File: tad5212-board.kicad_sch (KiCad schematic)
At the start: 11 parts, among them J1 Conn_01x10, J2 Conn_01x10, U1 XTAD5212IRGER

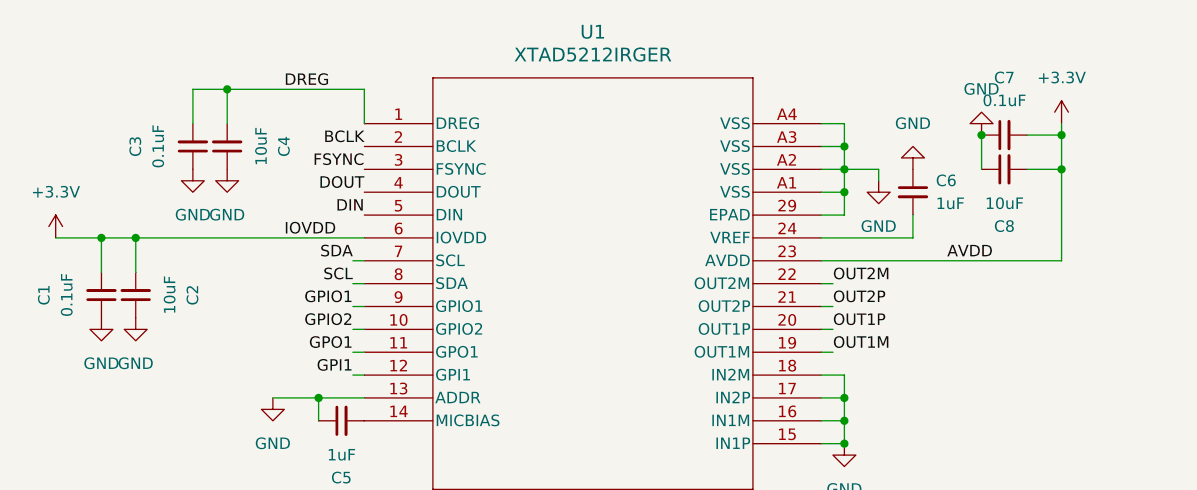
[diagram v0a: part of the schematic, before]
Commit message: v2 with hive compat footprints and fix i2c
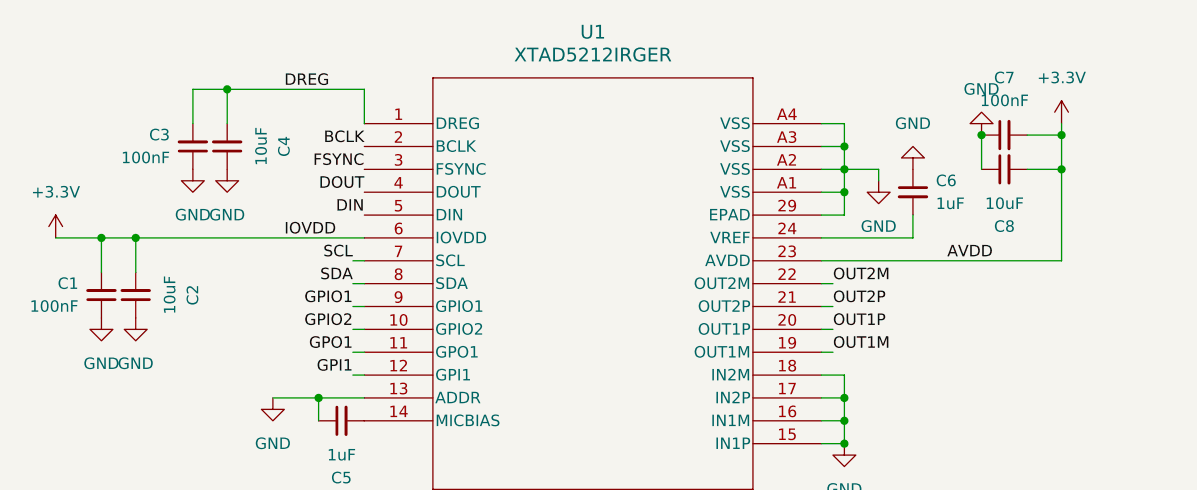
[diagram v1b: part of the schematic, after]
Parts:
- C1, C3, C7: value 0.1uF -> 100nF
- C2, C4, C8: footprint Capacitor_SMD:C_0603_1608Metric -> Capacitor_SMD:C_0805_2012Metric
- J1, J2: LCSC PN (none) -> C5383117
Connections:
- net SCL: now also U1.7 (SCL); no longer U1.8 (SDA)
- net SDA: now also U1.8 (SDA); no longer U1.7 (SCL)
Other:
- moved on the sheet: C1, C3

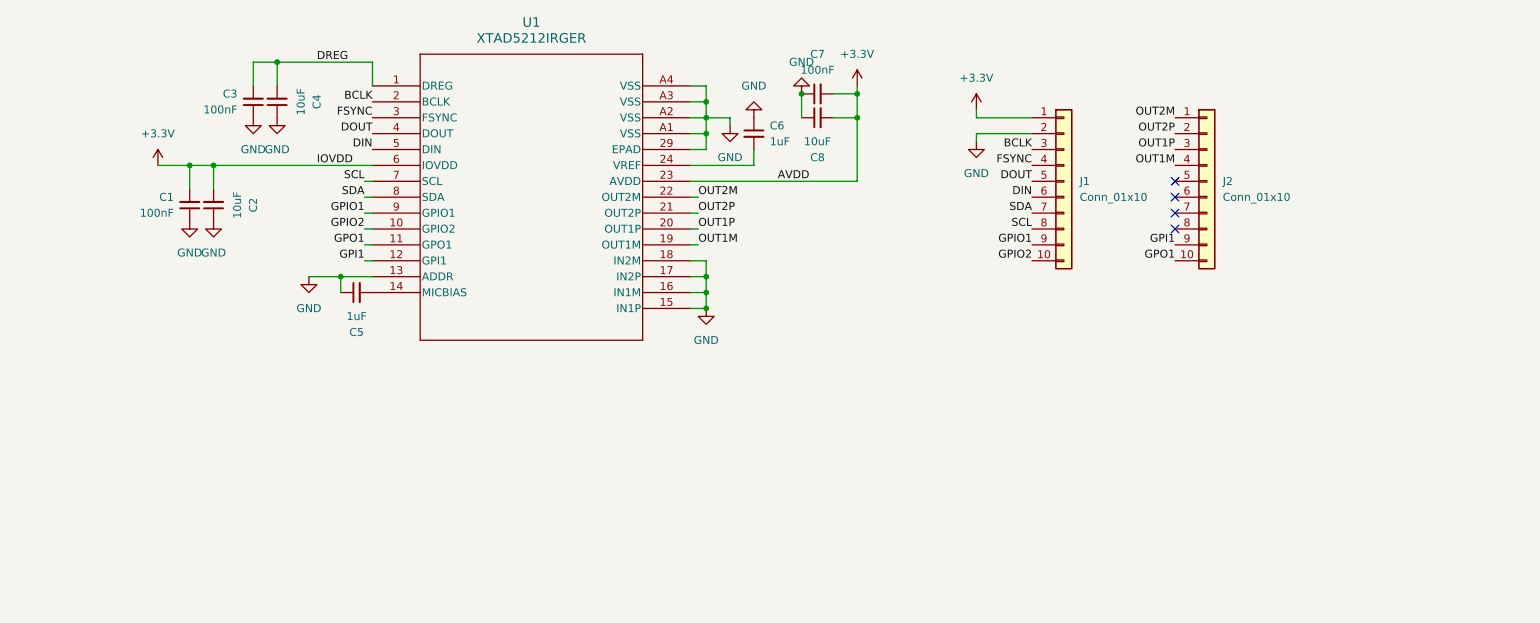
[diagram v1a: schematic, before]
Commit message: make 4-layer; add ldo
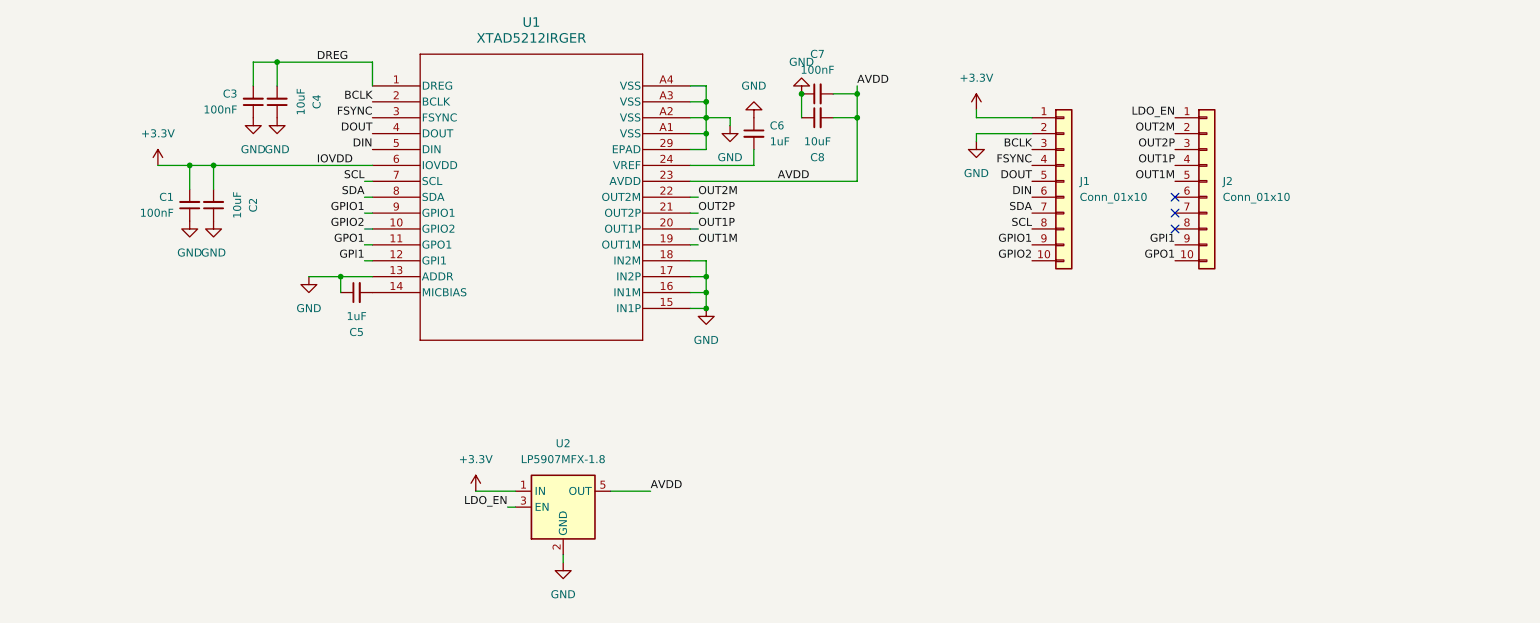
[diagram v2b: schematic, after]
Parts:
- added U2: LP5907MFX-1.8, Package_TO_SOT_SMD:SOT-23-5, symbol Regulator_Linear:LP5907MFX-1.8
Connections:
- net +3.3V: now also U2.1 (IN); no longer C7.2, C8.2, U1.23 (AVDD)
- net GND: now also U2.2 (GND)
- net OUT1M: now also J2.5 (Pin_5); no longer J2.4 (Pin_4)
- net OUT1P: now also J2.4 (Pin_4); no longer J2.3 (Pin_3)
- net OUT2M: now also J2.2 (Pin_2); no longer J2.1 (Pin_1)
- net OUT2P: now also J2.3 (Pin_3); no longer J2.2 (Pin_2)
- new net AVDD: C7.2, C8.2, U1.23 (AVDD), U2.5 (OUT)
- new net LDO_EN: J2.1 (Pin_1), U2.3 (EN)
- no-connect marks 4 -> 3

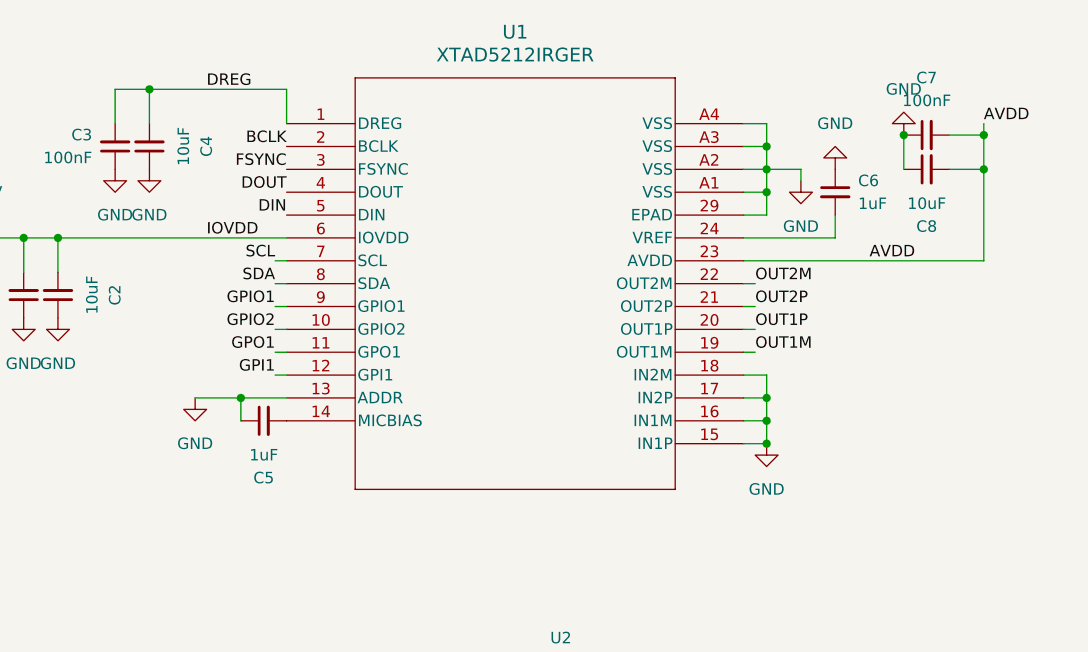
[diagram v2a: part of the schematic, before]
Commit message: add via stitching
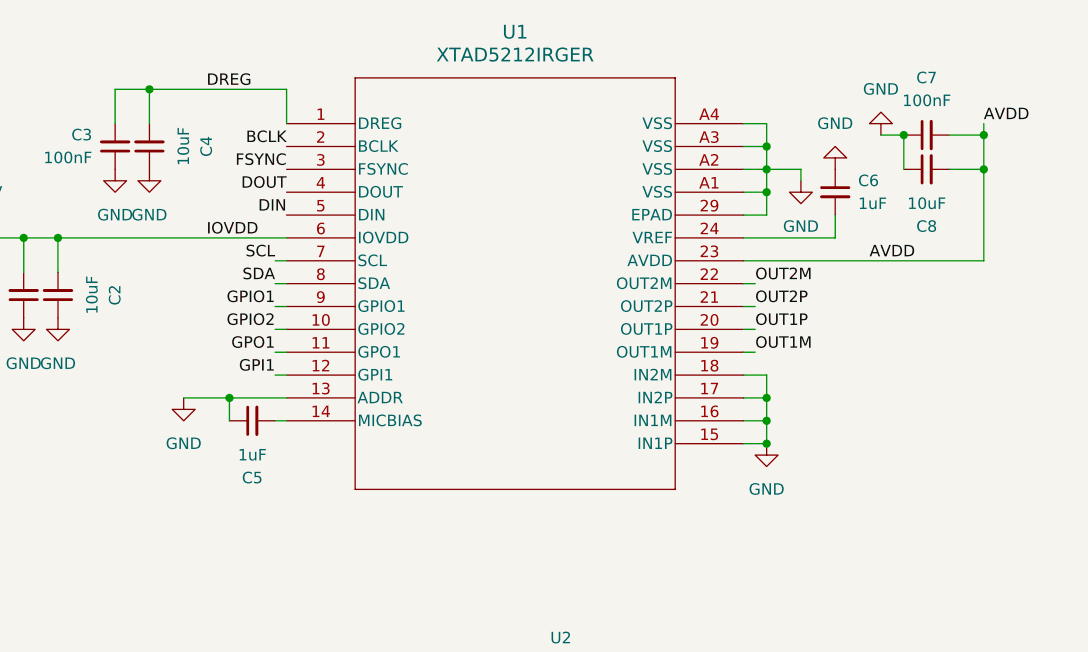
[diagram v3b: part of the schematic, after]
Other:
- moved on the sheet: C5
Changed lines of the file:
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@@
 	(paper "A4")
+	(junction
+		(at 57.15 64.77)
+		(diameter 0)
+		(color 0 0 0 0)
+	)
+	(junction
+		(at 60.96 64.77)
+		(diameter 0)
+		(color 0 0 0 0)
+	)
+	(junction
+		(at 163.83 57.15)
+		(diameter 0)
+		(color 0 0 0 0)
+	)
+	(junction
+		(at 139.7 57.15)
+		(diameter 0)
+		(color 0 0 0 0)
+	)
+	(junction
+		(at 139.7 85.09)
+		(diameter 0)
+		(color 0 0 0 0)
+	)
+	(junction
+		(at 139.7 59.69)
+		(diameter 0)
+		(color 0 0 0 0)
+	)
+	(junction
+		(at 139.7 82.55)
+		(diameter 0)
+		(color 0 0 0 0)
+	)
+	(junction
+		(at 80.01 82.55)
+		(diameter 0)
+		(color 0 0 0 0)
+	)
+	(junction
+		(at 139.7 87.63)
+		(diameter 0)
+		(color 0 0 0 0)
+	)
+	(junction
+		(at 163.83 53.34)
+		(diameter 0)
+		(color 0 0 0 0)
+	)
+	(junction
+		(at 71.12 48.26)
+		(diameter 0)
+		(color 0 0 0 0)
+	)
 	(junction
 		(at 154.94 53.34)
@@
 	)
 	(junction
-		(at 57.15 64.77)
-		(diameter 0)
-		(color 0 0 0 0)
-	)
-	(junction
-		(at 60.96 64.77)
-		(diameter 0)
-		(color 0 0 0 0)
-	)
-	(junction
-		(at 163.83 57.15)
-		(diameter 0)
-		(color 0 0 0 0)
-	)
-	(junction
-		(at 139.7 57.15)
-		(diameter 0)
-		(color 0 0 0 0)
-	)
-	(junction
-		(at 139.7 85.09)
-		(diameter 0)
-		(color 0 0 0 0)
-	)
-	(junction
-		(at 139.7 59.69)
-		(diameter 0)
-		(color 0 0 0 0)
-	)
-	(junction
-		(at 139.7 82.55)
-		(diameter 0)
-		(color 0 0 0 0)
-	)
-	(junction
-		(at 81.28 82.55)
-		(diameter 0)
-		(color 0 0 0 0)
-	)
-	(junction
-		(at 139.7 87.63)
-		(diameter 0)
-		(color 0 0 0 0)
-	)
-	(junction
-		(at 163.83 53.34)
-		(diameter 0)
-		(color 0 0 0 0)
-	)
-	(junction
-		(at 71.12 48.26)
-		(diameter 0)
-		(color 0 0 0 0)
-	)
-	(junction
 		(at 139.7 54.61)
 		(diameter 0)
@@
 	(wire
 		(pts
-			(xy 81.28 82.55) (xy 81.28 85.09)
+			(xy 80.01 82.55) (xy 80.01 85.09)
 		)
 		(stroke
@@
 	(wire
 		(pts
-			(xy 81.28 82.55) (xy 86.36 82.55)
+			(xy 80.01 82.55) (xy 86.36 82.55)
 		)
 		(stroke
@@
 	(wire
 		(pts
-			(xy 76.2 82.55) (xy 81.28 82.55)
+			(xy 74.93 82.55) (xy 80.01 82.55)
 		)
 		(stroke
@@
 	(wire
 		(pts
+			(xy 85.09 85.09) (xy 86.36 85.09)
+		)
+		(stroke
+			(width 0)
+			(type default)
+		)
+	)
+	(wire
+		(pts
 			(xy 60.96 64.77) (xy 86.36 64.77)
 		)
@@
 		(pts
 			(xy 60.96 64.77) (xy 60.96 68.58)
+		)
+		(stroke
+			(width 0)
+			(type default)
+		)
+	)
+	(wire
+		(pts
+			(xy 152.4 53.34) (xy 154.94 53.34)
 		)
 		(stroke
@@
 	(symbol
 		(lib_id "power:GND")
-		(at 154.94 53.34 180)
+		(at 152.4 53.34 180)
 		(unit 1)
 		(body_style 1)
@@
 		(fields_autoplaced yes)
 		(property "Reference" "#PWR013"
-			(at 154.94 46.99 0)
+			(at 152.4 46.99 0)
 			(hide yes)
 			(show_name no)
@@
 		)
 		(property "Value" "GND"
-			(at 154.94 48.26 0)
+			(at 152.4 48.26 0)
 			(show_name no)
 			(do_not_autoplace no)
@@
 		)
 		(property "Footprint" ""
-			(at 154.94 53.34 0)
+			(at 152.4 53.34 0)
 			(hide yes)
 			(show_name no)
@@
 		)
 		(property "Datasheet" ""
-			(at 154.94 53.34 0)
+			(at 152.4 53.34 0)
 			(hide yes)
 			(show_name no)
@@
 		)
 		(property "Description" "Power symbol creates a global label with name \"GND\" , ground"
-			(at 154.94 53.34 0)
+			(at 152.4 53.34 0)
 			(hide yes)
 			(show_name no)
@@
 	(symbol
 		(lib_id "Device:C_Small")
-		(at 83.82 85.09 90)
+		(at 82.55 85.09 90)
 		(mirror x)
 		(unit 1)
@@
 		(fields_autoplaced yes)
 		(property "Reference" "C5"
-			(at 83.8263 91.44 90)
+			(at 82.5563 91.44 90)
 			(show_name no)
 			(do_not_autoplace no)
@@
 		)
 		(property "Value" "1uF"
-			(at 83.8263 88.9 90)
+			(at 82.5563 88.9 90)
 			(show_name no)
 			(do_not_autoplace no)
@@
 		)
 		(property "Footprint" "Capacitor_SMD:C_0603_1608Metric"
-			(at 83.82 85.09 0)
+			(at 82.55 85.09 0)
 			(hide yes)
 			(show_name no)
@@
 		)
 		(property "Datasheet" ""
-			(at 83.82 85.09 0)
+			(at 82.55 85.09 0)
 			(hide yes)
 			(show_name no)
@@
 		)
 		(property "Description" "Unpolarized capacitor, small symbol"
-			(at 83.82 85.09 0)
+			(at 82.55 85.09 0)
 			(hide yes)
 			(show_name no)
@@
 	(symbol
 		(lib_id "power:GND")
-		(at 76.2 82.55 0)
+		(at 74.93 82.55 0)
 		(unit 1)
 		(body_style 1)
@@
 		(fields_autoplaced yes)
 		(property "Reference" "#PWR06"
-			(at 76.2 88.9 0)
+			(at 74.93 88.9 0)
 			(hide yes)
 			(show_name no)
@@
 		)
 		(property "Value" "GND"
-			(at 76.2 87.63 0)
+			(at 74.93 87.63 0)
 			(show_name no)
 			(do_not_autoplace no)
@@
 		)
 		(property "Footprint" ""
-			(at 76.2 82.55 0)
+			(at 74.93 82.55 0)
 			(hide yes)
 			(show_name no)
@@
 		)
 		(property "Datasheet" ""
-			(at 76.2 82.55 0)
+			(at 74.93 82.55 0)
 			(hide yes)
 			(show_name no)
@@
 		)
 		(property "Description" "Power symbol creates a global label with name \"GND\" , ground"
-			(at 76.2 82.55 0)
-			(hide yes)
-			(show_name no)
+			(at 74.93 82.55 0)
+			(hide yes)
+			(show_name no)

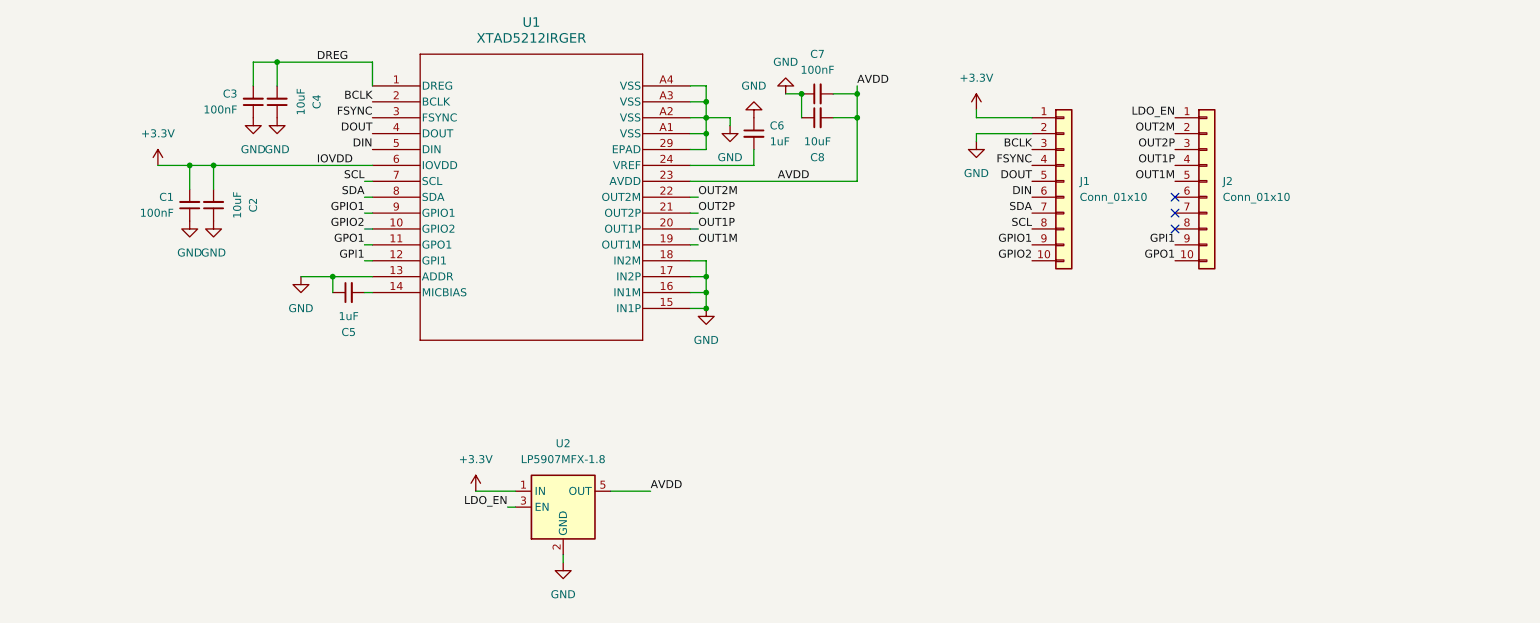
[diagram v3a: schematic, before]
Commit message: add oscillator
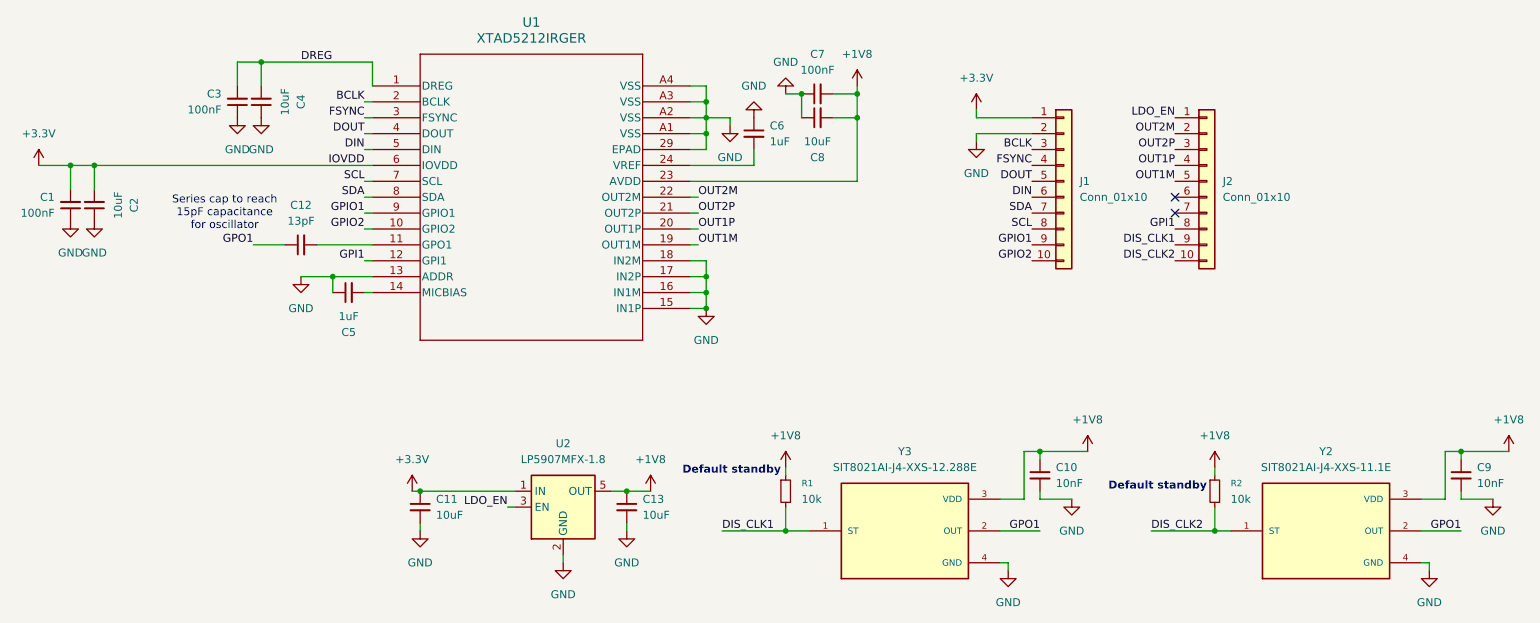
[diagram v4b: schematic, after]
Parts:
- added C10, C9: 10nF, Capacitor_SMD:C_0603_1608Metric, symbol Device:C_Small
- added C11, C13: 10uF, Capacitor_SMD:C_0805_2012Metric, symbol Device:C_Small
- added C12: 13pF, Capacitor_SMD:C_0603_1608Metric, symbol Device:C_Small
- added R1, R2: 10k, Resistor_SMD:R_0603_1608Metric, symbol Device:R_Small
- added Y2: SIT8021AI-J4-XXS-11.1E, SIT8021AI-J4-XXS-24.000000E:OSC_SIT8021AI-J4-XXS-24.000000E, symbol SIT8021AI-J4-XXS-24.000000E:SIT8021AI-J4-XXS-24.000000E
- added Y3: SIT8021AI-J4-XXS-12.288E, SIT8021AI-J4-XXS-24.000000E:OSC_SIT8021AI-J4-XXS-24.000000E, symbol SIT8021AI-J4-XXS-24.000000E:SIT8021AI-J4-XXS-24.000000E
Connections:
- net +3.3V: now also C11.1
- net GND: now also C10.2, C11.2, C13.2, C9.2, Y2.4 (GND), Y3.4 (GND)
- net GPI1: now also J2.8 (Pin_8); no longer J2.9 (Pin_9)
- net GPO1: now also C12.1, Y2.2 (OUT), Y3.2 (OUT); no longer J2.10 (Pin_10), U1.11 (GPO1)
- net AVDD renamed +1V8
- net +1V8: now also C10.1, C13.1, C9.1, R1.1, R2.1, Y2.3 (VDD), Y3.3 (VDD)
- new net: C12.2, U1.11 (GPO1)
- new net DIS_CLK1: J2.9 (Pin_9), R1.2, Y3.1 (ST)
- new net DIS_CLK2: J2.10 (Pin_10), R2.2, Y2.1 (ST)
- no-connect marks 3 -> 2
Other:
- note added: "Default standby"
- note added: "Series cap to reach 15pF capacitance for oscillator"
- moved on the sheet: C1, C2, C3, C4
